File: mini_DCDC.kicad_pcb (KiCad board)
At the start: 2 copper layers, 40 x 26 mm, 19 parts, among them J1 Pin, J2 Pin, J3 Pin, J4 Pin, J5 Pin, U1 MC34063AD

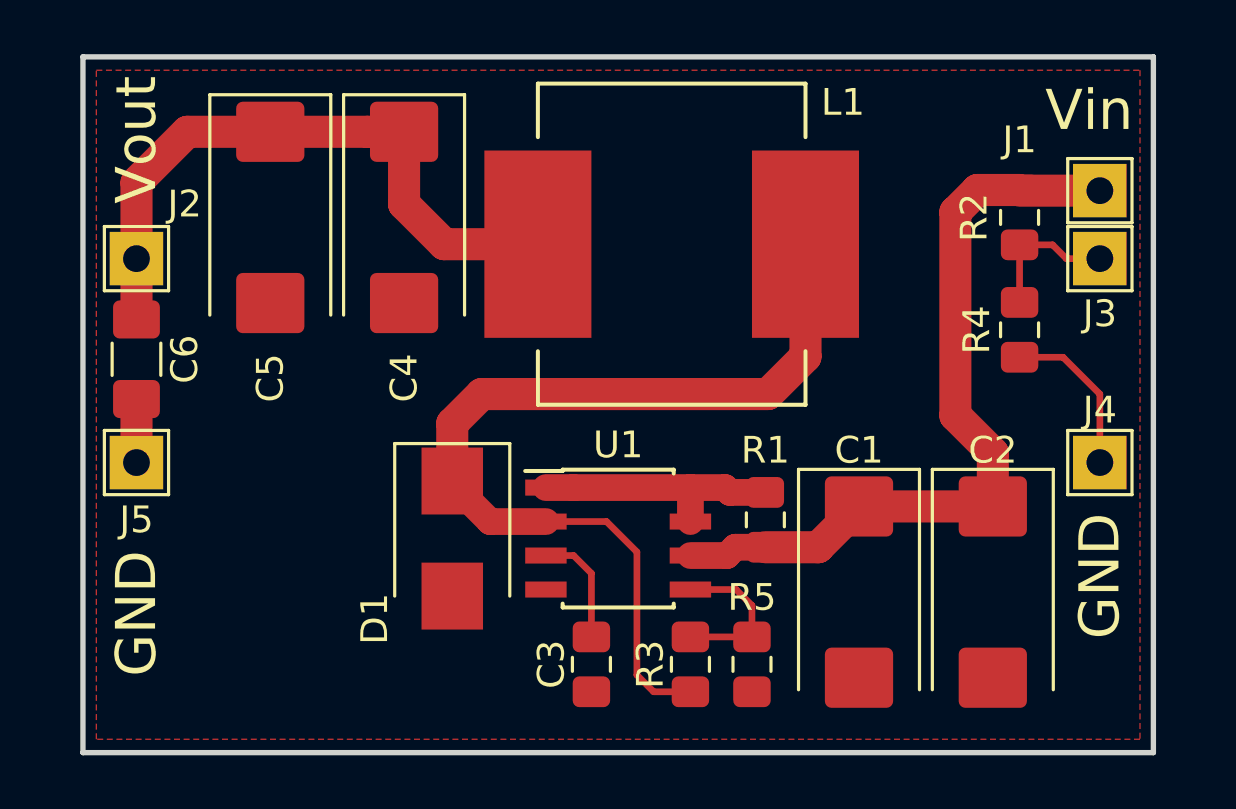
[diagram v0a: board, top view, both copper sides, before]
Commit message: - Исправлена ошибка с неправильным подключением цепи обратной связи; - Увеличена длина платы на 2 мм; - Плата переразведена с учетом изменений в схеме;
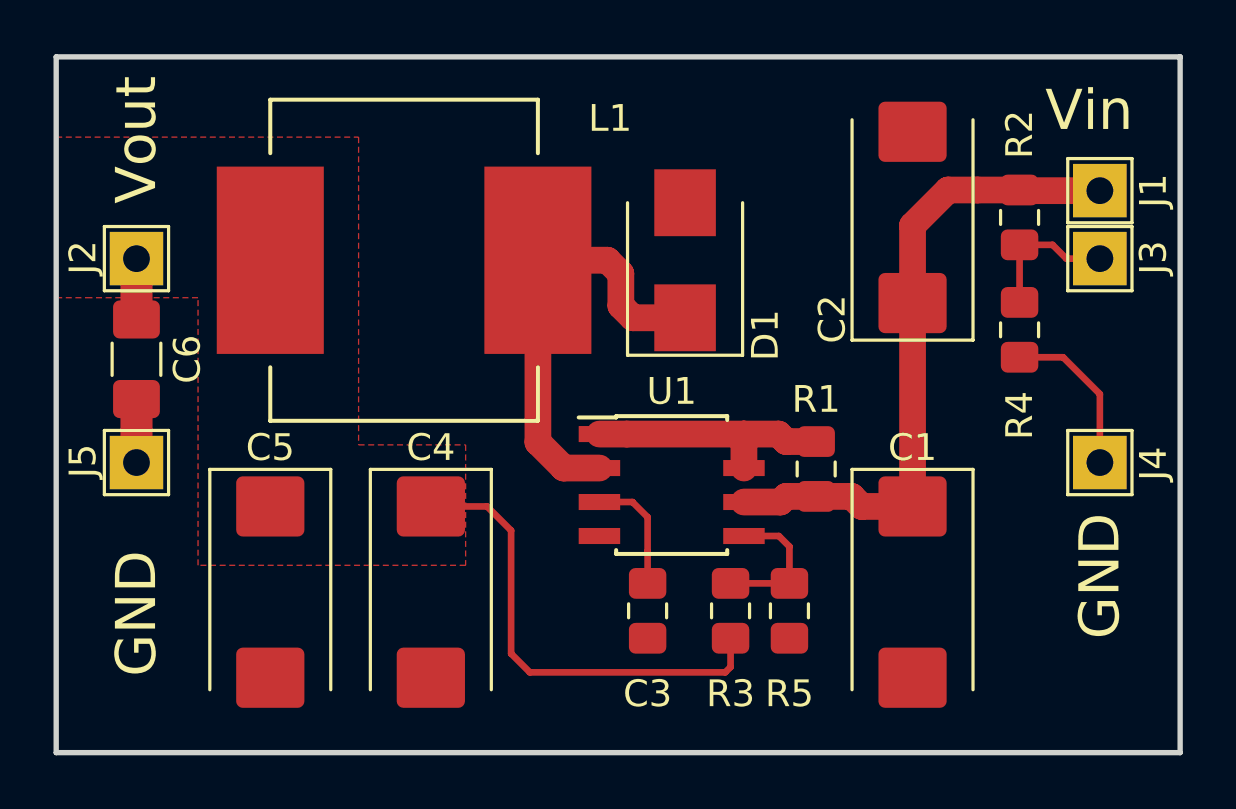
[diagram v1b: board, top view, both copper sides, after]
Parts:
- moved C2 14.3 mm to (81.0, 80.0), turned to 90 degrees
- moved C4 14.0 mm to (63.0, 94.0)
- moved C5 14.0 mm to (57.0, 94.0)
- moved D1 13.6 mm to (72.5, 81.6), turned to 90 degrees
- moved L1 10.0 mm to (67.0, 81.6)
- moved C3 2.90 mm to (71.1, 94.7)
- moved U1 2.83 mm to (72.0, 90.0)
- moved R1 2.69 mm to (77.4, 89.4)
- moved R3 2.50 mm to (74.2, 94.7)
- moved R5 2.44 mm to (76.4, 94.7)
- moved C1 2.00 mm to (81.0, 94.0)
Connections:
- R3 pad 1: Net-(D1-Pad1) -> +5V
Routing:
- net Net-(D1-Pad1): track 35.5 -> 16.6 mm
- net Vin: track 29.4 -> 24.8 mm
- net +5V: track 24.2 -> 19.9 mm
- net Net-(R3-Pad2): track 6.02 -> 5.44 mm
- added copper zone on F.Cu, net +5V
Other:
- board size 40 x 26 mm -> 42 x 26 mm
